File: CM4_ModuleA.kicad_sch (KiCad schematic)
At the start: 2 parts

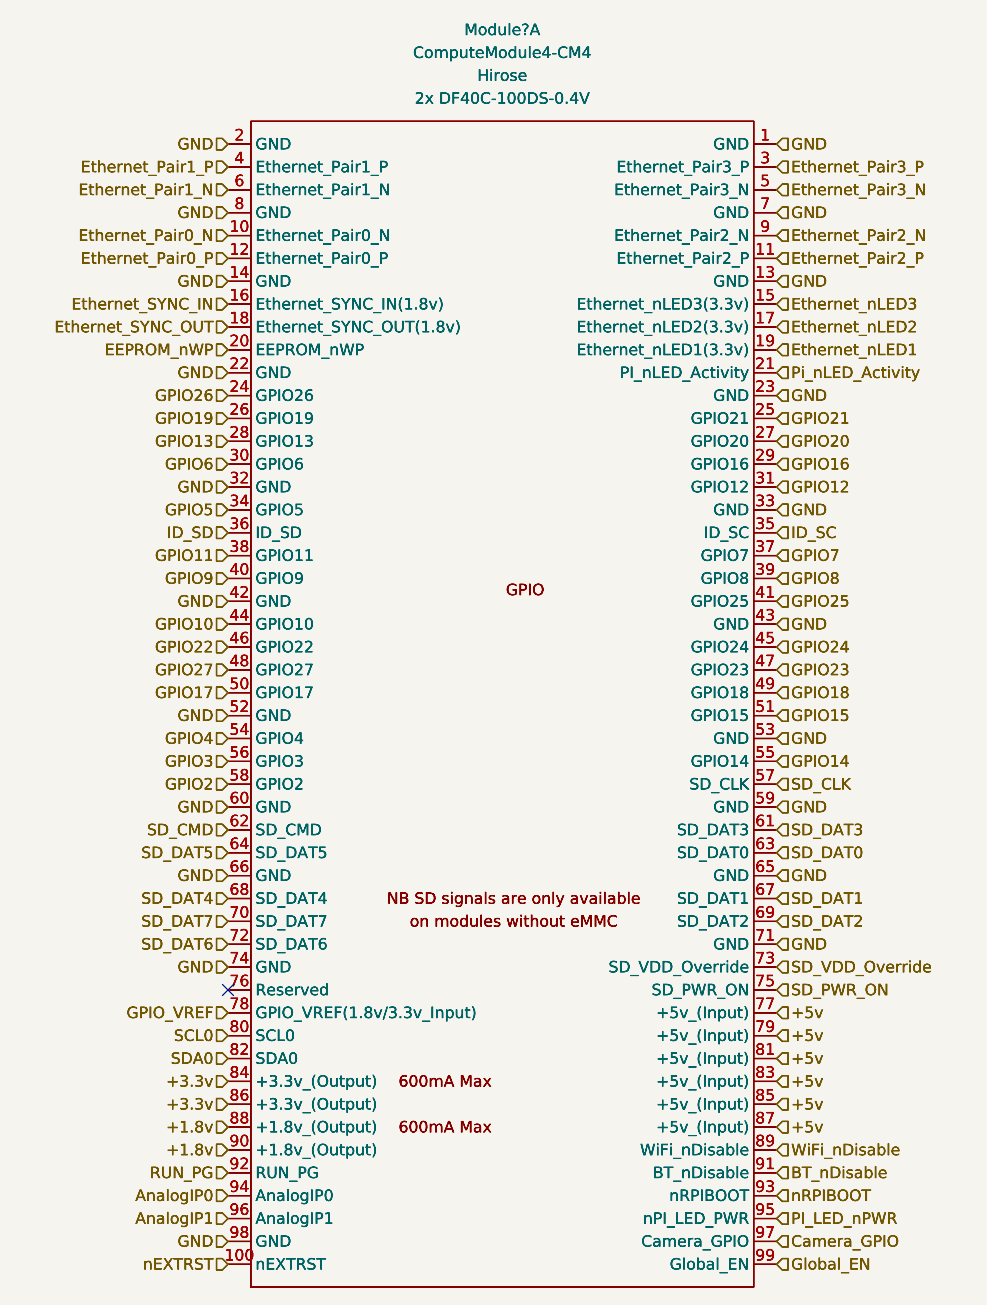
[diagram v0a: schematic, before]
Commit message: PCB ready to trace
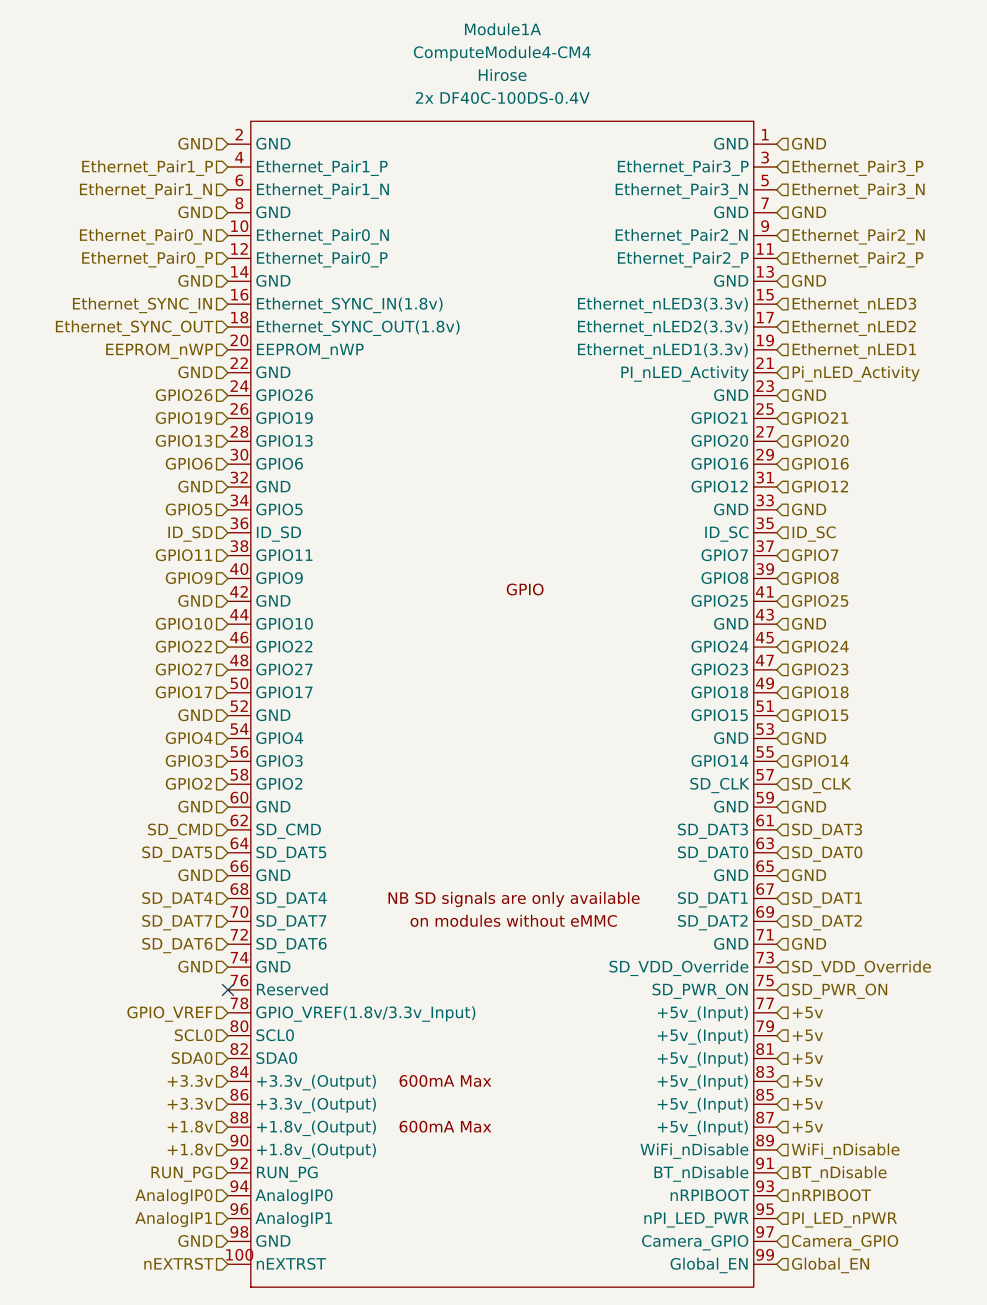
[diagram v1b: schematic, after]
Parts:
- removed Module?: ComputeModule4-CM4, CM4IO:Raspberry-Pi-4-Compute-Module, symbol CM4IO:ComputeModule4-CM4
- gave numbers to parts that had none: 1
